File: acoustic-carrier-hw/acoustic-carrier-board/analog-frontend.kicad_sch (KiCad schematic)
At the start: 99 parts, among them J1001 BWU.FL-IPEX1, J1002 BWU.FL-IPEX1, J1003 BWU.FL-IPEX1, J1005 BWU.FL-IPEX1, J1006 BWU.FL-IPEX1, J1007 8P8C_Shielded, J1008 BWU.FL-IPEX1, J1009 BWU.FL-IPEX1, J1010 BWU.FL-IPEX1, U1001 MS9280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

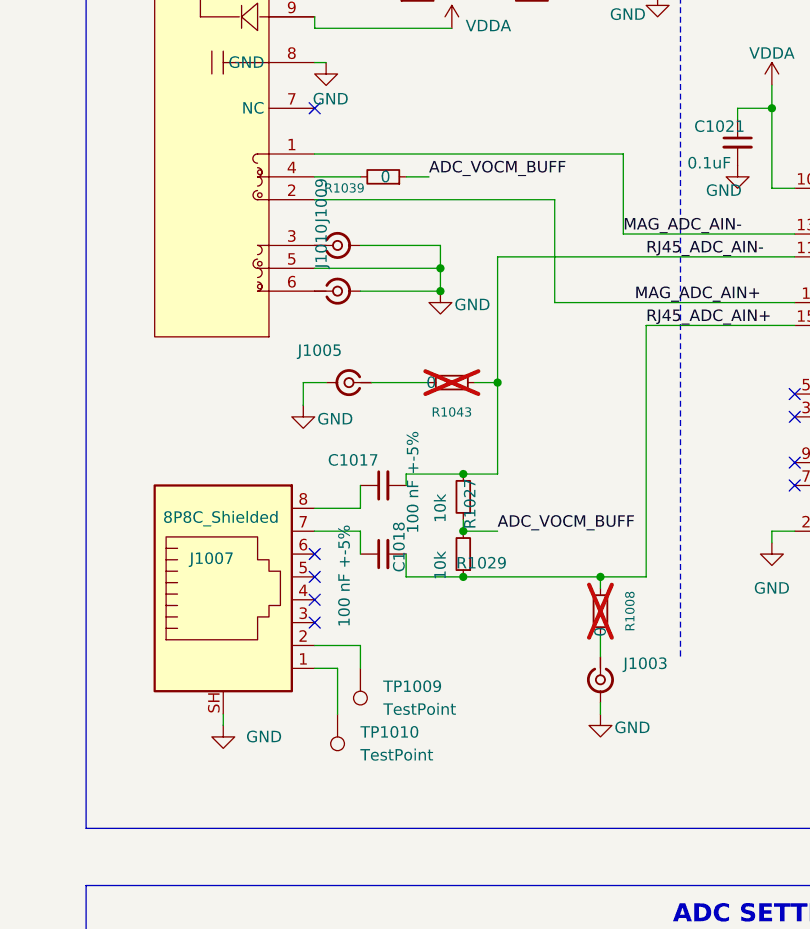
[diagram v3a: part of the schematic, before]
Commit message: [carrier] Fixed most routing errors
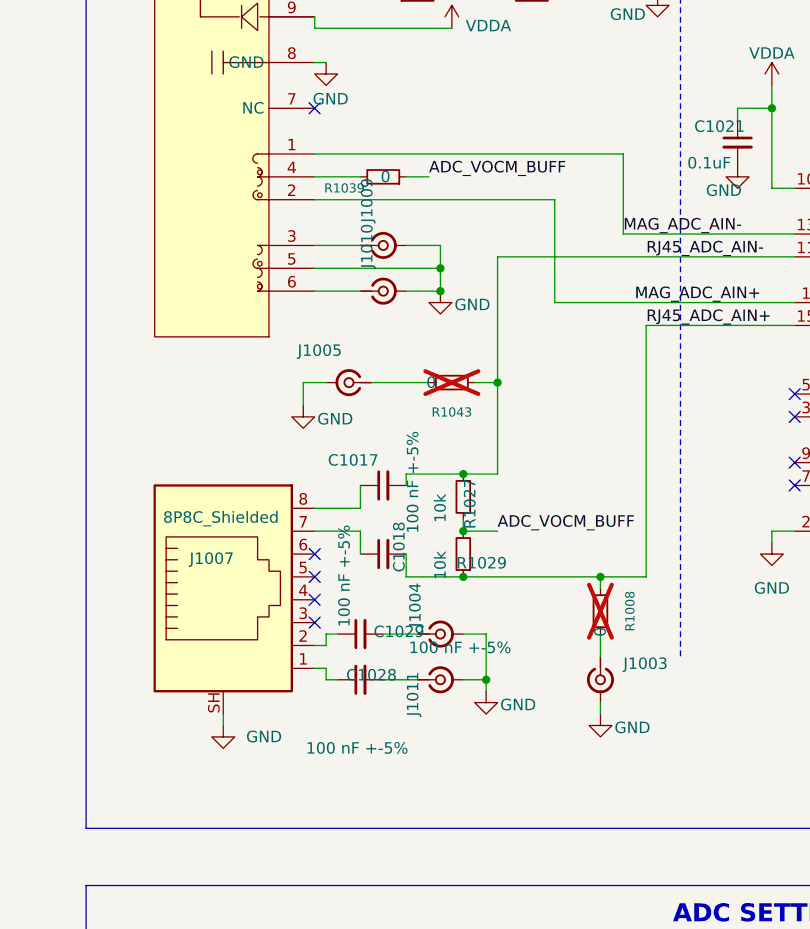
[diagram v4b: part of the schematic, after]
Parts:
- removed TP1009, TP1010: TestPoint, TestPoint:TestPoint_Loop_D1.80mm_Drill1.0mm_Beaded, symbol Connector:TestPoint
- added C1028, C1029: 100 nF +-5%, Capacitor_SMD:C_0603_1608Metric_Pad1.08x0.95mm_HandSolder, symbol Device:C_Small
- added J1004, J1011: BWU.FL-IPEX1, iw-connector:BWU.FL-IPEX1, symbol Connector:Conn_Coaxial_Small
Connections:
- net GND: now also J1004.2 (Ext), J1011.2 (Ext)
- net at J1007.2: now also C1029.1
- net at J1007.1: now also C1028.1
- new net: C1029.2, J1004.1 (In)
- new net: C1028.2, J1011.1 (In)
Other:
- moved on the sheet: J1009, J1010
